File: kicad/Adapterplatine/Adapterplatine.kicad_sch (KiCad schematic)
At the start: 38 parts, among them J1 Conn_02x10_Top_Bottom, J10 Conn_01x04_Pin, J11 Conn_01x03_Pin, J12 Conn_01x02_Pin, J13 Conn_01x05_Pin, J14 Conn_01x02_Pin, J15 Conn_01x02_Pin, J16 Conn_01x05_Pin, J17 Conn_01x05_Pin, J18 Conn_01x05_Pin, J19 Conn_01x05_Pin, J2 DE9_Socket, J20 Conn_01x05_Pin, J21 Conn_01x05_Pin, J22 Conn_01x02_Pin, J23 Conn_01x02_Pin, J24 Conn_01x02_Pin, J25 Conn_01x02_Pin, J26 Conn_01x02_Pin, J27 Conn_01x05_Pin, J28 Conn_01x05_Pin, J29 Conn_01x02_Pin, J3 DE9_Pins, J30 Conn_01x05_Pin, J31 Conn_01x05_Pin, J32 Conn_01x05_Pin, J33 Conn_02x05_Top_Bottom, J34 Conn_01x02_Pin, J35 Conn_01x02_Pin, J4 DE9_Pins, J5 Conn_01x04_Pin, J6 Conn_01x04_Pin, J7 Conn_01x04_Pin, J8 Conn_01x04_Pin, J9 Conn_01x04_Pin

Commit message: Update KiCad
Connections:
- net at R3.1: now also R1.1, R2.1
- net GND: now reaches J35.2 (Pin_2)
- net GND: now also J33.5 (Pin_5), J34.2 (Pin_2)
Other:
- moved on the sheet: R1, R2, R3

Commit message: Adapterplatine weitergeführt/ Doku F421
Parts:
- added FAN0, FAN1, FAN2, X38__1, X44__g1, X44__r1, X48__PT1000_1, X48__PT1000_2: Conn_01x02_Pin, Connector_JST:JST_XH_B2B-XH-A_1x02_P2.50mm_Vertical, symbol Connector:Conn_01x02_Pin
- added I2C1: Conn_01x04_Pin, Connector_PinHeader_2.54mm:PinHeader_1x04_P2.54mm_Vertical, symbol Connector:Conn_01x04_Pin
- added Raspi_1, Raspi_2: Conn_01x05_Pin, Connector_PinHeader_2.54mm:PinHeader_1x05_P2.54mm_Vertical, symbol Connector:Conn_01x05_Pin
- added X10__1, X9__1: Conn_01x04_Pin, Connector_JST:JST_XH_B4B-XH-A_1x04_P2.50mm_Vertical, symbol Connector:Conn_01x04_Pin
- added X12__1, X13__1, X15__1, X37__1, X39__1, X48__Servo1, X_EndStop4, X_EndStop5, X_EndStop6: Conn_01x03_Pin, Connector_JST:JST_XH_B3B-XH-A_1x03_P2.50mm_Vertical, symbol Connector:Conn_01x03_Pin
- added X1__1, X3__1: Conn_01x02_Pin, Connector_Phoenix_MSTB:PhoenixContact_MSTBA_2,5_2-G_1x02_P5.00mm_Horizontal, symbol Connector:Conn_01x02_Pin
- added X44__y1, X44_b1: Conn_01x04_Pin, Connector_Molex:Molex_KK-254_AE-6410-04A_1x04_P2.54mm_Vertical, symbol Connector:Conn_01x04_Pin
- added X46__1: Conn_02x05_Top_Bottom, Connector_IDC:IDC-Header_2x05_P2.54mm_Vertical, symbol Connector_Generic:Conn_02x05_Top_Bottom
- added X5__1, X6__1, X7__1: Conn_01x04_Pin, Connector_JST:JST_VH_B4P-VH_1x04_P3.96mm_Vertical, symbol Connector:Conn_01x04_Pin
- X46: renamed from J33; footprint Connector_PinHeader_2.54mm:PinHeader_2x05_P2.54mm_Vertical -> Connector_IDC:IDC-Header_2x05_P2.54mm_Vertical
- renumbered J13 to J2, J10 to J3, J11 to J4, R1 to R_X12, R2 to R_X13, R3 to R_X15, J34 to X1, J6 to X10, J19 to X12, J20 to X13, J31 to X15, J21 to X16, J15 to X20, J12 to X22, J22 to X23, J29 to X25_1, J18 to X28_1, J32 to X29_1, J35 to X3, J16 to X30, J17 to X31, J3 to X36A1, J2 to X36B1, J25 to X37, J23 to X38, J24 to X39, J14 to X40, J28 to X43, J27 to X44, J4 to X45, J1 to X48, J7 to X5, J30 to X52, J26 to X56, J8 to X6, J9 to X7, J5 to X9
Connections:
- net GND: now also X12.2 (Pin_2), X12.4 (Pin_4), X13.2 (Pin_2), X13.4 (Pin_4), X15.2 (Pin_2), X15.4 (Pin_4), X29_1.1 (Pin_1), X29_1.5 (Pin_5), I2C1.2 (Pin_2), Raspi_1.3 (Pin_3), Raspi_2.3 (Pin_3), X12__1.2 (Pin_2), X13__1.2 (Pin_2), X15__1.2 (Pin_2), X1__1.2 (Pin_2), X3__1.2 (Pin_2), X46__1.6 (Pin_6)
- net at R_X15.2: now also X15.1 (Pin_1)
- net at X44.1 (Pin_1): now also X44_b1.1 (Pin_1)
- net at X44.2 (Pin_2): now also X44__g1.1 (Pin_1), X44__r1.1 (Pin_1), X44__y1.3 (Pin_3), X44_b1.3 (Pin_3)
- net at X44.3 (Pin_3): now also X44__y1.1 (Pin_1)
- net at X44.4 (Pin_4): now also X44__g1.2 (Pin_2)
- net at X44.5 (Pin_5): now also X44__r1.2 (Pin_2)
- net at X29_1.2 (Pin_2): now also I2C1.1 (Pin_1)
- net at X29_1.3 (Pin_3): now also I2C1.3 (Pin_3)
- net at X29_1.4 (Pin_4): now also I2C1.4 (Pin_4)
- net at X9.1 (Pin_1): now also X9__1.2 (Pin_2)
- net at X9.2 (Pin_2): now also X9__1.1 (Pin_1)
- net at X9.3 (Pin_3): now also X9__1.4 (Pin_4)
- net at X9.4 (Pin_4): now also X9__1.3 (Pin_3)
- net at X10.1 (Pin_1): now also X10__1.2 (Pin_2)
- net at X10.2 (Pin_2): now also X10__1.1 (Pin_1)
- net at X10.3 (Pin_3): now also X10__1.4 (Pin_4)
- net at X10.4 (Pin_4): now also X10__1.3 (Pin_3)
- net at X3.1 (Pin_1): now also X3__1.1 (Pin_1)
- net at X12.1 (Pin_1): now also R_X12.1
- net at X12.5 (Pin_5): now also X12__1.3 (Pin_3)
- net at R_X13.2: now also X13__1.1 (Pin_1)
- net at X37.1 (Pin_1): now also X37__1.2 (Pin_2)
- net at X37.2 (Pin_2): now also X37__1.3 (Pin_3)
- net at X39.1 (Pin_1): now also X39__1.2 (Pin_2)
- net at X39.2 (Pin_2): now also X39__1.3 (Pin_3)
- net at X7.1 (Pin_1): now also X7__1.2 (Pin_2)
- net at X7.2 (Pin_2): now also X7__1.1 (Pin_1)
- net at X7.3 (Pin_3): now also X7__1.4 (Pin_4)
- net at X7.4 (Pin_4): now also X7__1.3 (Pin_3)
- net GND TOOL: now reaches X48.1 (Pin_1)
- net GND TOOL: now also X48.15 (Pin_15), X48.16 (Pin_16), X48.2 (Pin_2), X48.8 (Pin_8)
- net at X48.10 (Pin_10): now also X48__Servo1.1 (Pin_1)
- net VIN Tool1: now reaches X48.11 (Pin_11)
- net VIN Tool1: now also X48.12 (Pin_12)
- net at X48.13 (Pin_13): now also X48__PT1000_1.2 (Pin_2)
- net at X48.14 (Pin_14): now also X48__PT1000_2.2 (Pin_2)
- net VIN Tool0: now reaches X48.17 (Pin_17)
- net VIN Tool0: now also X48.18 (Pin_18)
- net at X48.19 (Pin_19): now also X48__PT1000_2.1 (Pin_1)
- net at X48.20 (Pin_20): now also X48__PT1000_1.1 (Pin_1)
- net at X48.4 (Pin_4): now also FAN1.1 (Pin_1)
- net at X48.6 (Pin_6): now also FAN2.2 (Pin_2)
- net at X48.7 (Pin_7): now also X48__Servo1.2 (Pin_2)
- net at X48.9 (Pin_9): now also FAN1.2 (Pin_2), FAN2.1 (Pin_1), X48__Servo1.3 (Pin_3)
- net at X15.5 (Pin_5): now also X15__1.3 (Pin_3)
- net at X13.1 (Pin_1): now also R_X13.1
- net at X13.5 (Pin_5): now also X13__1.3 (Pin_3)
- net at X1.1 (Pin_1): now also X1__1.1 (Pin_1)
- net at X46.1 (Pin_1): now also X46__1.1 (Pin_1)
- net at X46.10 (Pin_10): now also X46__1.10 (Pin_10)
- net at X46.2 (Pin_2): now also X46__1.2 (Pin_2)
- net at X46.3 (Pin_3): now also X46__1.3 (Pin_3)
- net at X46.7 (Pin_7): now also X46__1.7 (Pin_7)
- net at R_X12.2: now also X12__1.1 (Pin_1)
- net at X5.1 (Pin_1): now also X5__1.2 (Pin_2)
- net at X5.2 (Pin_2): now also X5__1.1 (Pin_1)
- net at X5.3 (Pin_3): now also X5__1.4 (Pin_4)
- net at X5.4 (Pin_4): now also X5__1.3 (Pin_3)
- net at X38.1 (Pin_1): now also X38__1.1 (Pin_1)
- net at X38.2 (Pin_2): now also X38__1.2 (Pin_2)
- net at X6.1 (Pin_1): now also X6__1.2 (Pin_2)
- net at X6.2 (Pin_2): now also X6__1.1 (Pin_1)
- net at X6.3 (Pin_3): now also X6__1.4 (Pin_4)
- net at X6.4 (Pin_4): now also X6__1.3 (Pin_3)
- new net: R_X15.1, X15__1.1 (Pin_1)
- new net: Raspi_1.1 (Pin_1), Raspi_2.1 (Pin_1)
- new net: Raspi_1.2 (Pin_2), Raspi_2.2 (Pin_2)
- new net: Raspi_1.4 (Pin_4), Raspi_2.4 (Pin_4)
- new net: Raspi_1.5 (Pin_5), Raspi_2.5 (Pin_5)
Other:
- moved on the sheet: R_X12, R_X13, R_X15, X12, X13, X15, X16, X23, X25_1, X28_1, X29_1, X37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

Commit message: Doku F421/ Klipper ython modul erstellt/ KiCad Adapterplatine
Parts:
- added X48_Tool0, X48_Tool1: Conn_01x02_Pin, Connector_Phoenix_MSTB:PhoenixContact_MSTBA_2,5_2-G_1x02_P5.00mm_Horizontal, symbol Connector:Conn_01x02_Pin
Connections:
- net GND TOOL: now also X48_Tool0.1 (Pin_1), X48_Tool1.1 (Pin_1)
- net VIN Tool0: now also X48_Tool0.2 (Pin_2)
- net VIN Tool1: now also X48_Tool1.2 (Pin_2)

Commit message: Adapterplatinen Update
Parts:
- removed X_EndStop4, X_EndStop5: Conn_01x03_Pin, Connector_JST:JST_XH_B3B-XH-A_1x03_P2.50mm_Vertical, symbol Connector:Conn_01x03_Pin
- added MAX31865_IN1: Conn_01x08_Pin, Connector_PinSocket_2.54mm:PinSocket_1x08_P2.54mm_Vertical, symbol Connector:Conn_01x08_Pin
- added MAX31865_OUT1: Conn_01x04_Pin, Connector_PinSocket_2.54mm:PinSocket_1x04_P2.54mm_Vertical, symbol Connector:Conn_01x04_Pin
- added PowerOn1: Conn_01x02_Pin, Connector_PinHeader_2.54mm:PinHeader_1x02_P2.54mm_Vertical, symbol Connector:Conn_01x02_Pin
- added SPI4: Conn_02x04_Top_Bottom, Connector_PinHeader_2.54mm:PinHeader_2x04_P2.54mm_Vertical, symbol Connector_Generic:Conn_02x04_Top_Bottom
- added T_Bauraum1, T_HeizE1, T_Heizbett1: Conn_01x02_Pin, Connector_JST:JST_XH_B2B-XH-A_1x02_P2.50mm_Vertical, symbol Connector:Conn_01x02_Pin
- renumbered X_EndStop6 to Not_Aus1
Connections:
- net GND: now also X43.1 (Pin_1), MAX31865_IN1.2 (Pin_2), SPI4.1 (Pin_1), SPI4.4 (Pin_4)
- net at X29_1.2 (Pin_2): no longer I2C1.1 (Pin_1)
- net at X29_1.3 (Pin_3): now also I2C1.4 (Pin_4); no longer I2C1.3 (Pin_3)
- net at X29_1.4 (Pin_4): now also I2C1.3 (Pin_3); no longer I2C1.4 (Pin_4)
- net at FAN0.1 (Pin_1): now also X25_1.1 (Pin_1)
- net at FAN0.2 (Pin_2): now also X25_1.2 (Pin_2)
- net at X23.1 (Pin_1): now also T_Bauraum1.1 (Pin_1)
- net at X23.2 (Pin_2): now also T_Bauraum1.2 (Pin_2)
- net at X20.1 (Pin_1): now also T_HeizE1.1 (Pin_1)
- net at X20.2 (Pin_2): now also T_HeizE1.2 (Pin_2)
- net at X43.2 (Pin_2): now also PowerOn1.1 (Pin_1)
- net at X43.4 (Pin_4): now also PowerOn1.2 (Pin_2)
- net at X43.5 (Pin_5): now also I2C1.1 (Pin_1), SPI4.8 (Pin_8)
- net at X22.1 (Pin_1): now also MAX31865_OUT1.2 (Pin_2)
- net at X22.2 (Pin_2): now also MAX31865_OUT1.3 (Pin_3)
- net at Not_Aus1.2 (Pin_2): now also X16.4 (Pin_4)
- net at Not_Aus1.3 (Pin_3): now also X16.5 (Pin_5)
- net at X56.1 (Pin_1): now also T_Heizbett1.1 (Pin_1)
- net at X56.2 (Pin_2): now also T_Heizbett1.2 (Pin_2)
- new net: MAX31865_IN1.4 (Pin_4), SPI4.2 (Pin_2)
- new net: MAX31865_IN1.5 (Pin_5), SPI4.3 (Pin_3)
- new net: MAX31865_IN1.1 (Pin_1), SPI4.5 (Pin_5)
- new net: MAX31865_IN1.7 (Pin_7), SPI4.6 (Pin_6)
- new net: MAX31865_IN1.6 (Pin_6), SPI4.7 (Pin_7)
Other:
- moved on the sheet: FAN0, Not_Aus1, Raspi_1

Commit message: Kicad update
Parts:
- FAN0, FAN1, FAN2, PowerOn1, T_Bauraum1, T_HeizE1, T_Heizbett1, X1, X1__1, X20, X22, X23, X25_1, X3, X37, X38, X38__1, X39, X3__1, X40, X44__g1, X44__r1, X48_Tool0, X48_Tool1, X48__PT1000_1, X48__PT1000_2, X56: symbol Connector:Conn_01x02_Pin -> Connector_Generic:Conn_01x02
- J2, Raspi_1, Raspi_2, X12, X13, X15, X16, X28_1, X29_1, X30, X31, X43, X44, X52: symbol Connector:Conn_01x05_Pin -> Connector_Generic:Conn_01x05
- X36A1, X45: symbol Connector:DE9_Pins -> Connector:DE9_Pins_MountingHoles
- X36B1: symbol Connector:DE9_Socket -> Connector:DE9_Socket_MountingHoles
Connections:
- net GND: no longer X15.2 (Pin_2), X15.4 (Pin_4), X29_1.1 (Pin_1), X29_1.5 (Pin_5)
- net at R_X15.2: no longer X15.1 (Pin_1)
- net at X29_1.3 (Pin_3): no longer I2C1.4 (Pin_4)
- net at X29_1.4 (Pin_4): no longer I2C1.3 (Pin_3)
- net +5V: now reaches I2C1.1 (Pin_1), SPI4.8 (Pin_8), X43.5 (Pin_5)
- net +5V: now also R_X13.1, X13.1 (Pin_1)
- net at Not_Aus1.2 (Pin_2), X16.4 (Pin_4): now also X16.3 (Pin_3)
- net at X15.5 (Pin_5): no longer X15__1.3 (Pin_3)
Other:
- moved on the sheet: J3, J4, Not_Aus1, R_X12, R_X13, X12__1, X13__1, X37__1, X39__1, X44__y1, X44_b1

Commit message: Adapterplatine sortiert
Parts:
- removed FAN0, FAN1, FAN2, T_Bauraum1, T_HeizE1, T_Heizbett1, X38__1, X44__g1, X44__r1, X48__PT1000_1, X48__PT1000_2: Conn_01x02_Pin, Connector_JST:JST_XH_B2B-XH-A_1x02_P2.50mm_Vertical, symbol Connector_Generic:Conn_01x02
- removed I2C1, J3: Conn_01x04_Pin, Connector_PinHeader_2.54mm:PinHeader_1x04_P2.54mm_Vertical, symbol Connector:Conn_01x04_Pin
- removed J2, Raspi_1, Raspi_2, X12, X13, X15, X16, X28_1, X29_1, X30, X31, X43, X44: Conn_01x05_Pin, Connector_PinHeader_2.54mm:PinHeader_1x05_P2.54mm_Vertical, symbol Connector_Generic:Conn_01x05
- removed J4: Conn_01x03_Pin, Connector_PinHeader_2.54mm:PinHeader_1x03_P2.54mm_Vertical, symbol Connector:Conn_01x03_Pin
- removed MAX31865_IN1: Conn_01x08_Pin, Connector_PinSocket_2.54mm:PinSocket_1x08_P2.54mm_Vertical, symbol Connector:Conn_01x08_Pin
- removed MAX31865_OUT1: Conn_01x04_Pin, Connector_PinSocket_2.54mm:PinSocket_1x04_P2.54mm_Vertical, symbol Connector:Conn_01x04_Pin
- removed Not_Aus1, X12__1, X13__1, X15__1, X37__1, X39__1, X48__Servo1: Conn_01x03_Pin, Connector_JST:JST_XH_B3B-XH-A_1x03_P2.50mm_Vertical, symbol Connector:Conn_01x03_Pin
- removed PowerOn1, X20, X22, X23, X25_1, X37, X38, X39, X56: Conn_01x02_Pin, Connector_PinHeader_2.54mm:PinHeader_1x02_P2.54mm_Vertical, symbol Connector_Generic:Conn_01x02
- removed R_X12, R_X13, R_X15: 220, Resistor_THT:R_Axial_DIN0207_L6.3mm_D2.5mm_P2.54mm_Vertical, symbol Device:R
- removed SPI4: Conn_02x04_Top_Bottom, Connector_PinHeader_2.54mm:PinHeader_2x04_P2.54mm_Vertical, symbol Connector_Generic:Conn_02x04_Top_Bottom
- removed X1, X1__1, X3, X3__1, X48_Tool0, X48_Tool1: Conn_01x02_Pin, Connector_Phoenix_MSTB:PhoenixContact_MSTBA_2,5_2-G_1x02_P5.00mm_Horizontal, symbol Connector_Generic:Conn_01x02
- removed X10, X5, X6, X7, X9: Conn_01x04_Pin, Connector_Phoenix_MSTB:PhoenixContact_MSTBVA_2,5_4-G-5,08_1x04_P5.08mm_Vertical, symbol Connector:Conn_01x04_Pin
- removed X10__1, X9__1: Conn_01x04_Pin, Connector_JST:JST_XH_B4B-XH-A_1x04_P2.50mm_Vertical, symbol Connector:Conn_01x04_Pin
- removed X36B1: DE9_Socket, Connector_Dsub:DSUB-9_Socket_Vertical_P2.77x2.84mm_MountingHoles, symbol Connector:DE9_Socket_MountingHoles
- removed X44__y1, X44_b1: Conn_01x04_Pin, Connector_Molex:Molex_KK-254_AE-6410-04A_1x04_P2.54mm_Vertical, symbol Connector:Conn_01x04_Pin
- removed X46, X46__1: Conn_02x05_Top_Bottom, Connector_IDC:IDC-Header_2x05_P2.54mm_Vertical, symbol Connector_Generic:Conn_02x05_Top_Bottom
- removed X48: Conn_02x10_Top_Bottom, Connector_Molex:Molex_Micro-Fit_3.0_43045-2012_2x10_P3.00mm_Vertical, symbol Connector_Generic:Conn_02x10_Top_Bottom
- removed X5__1, X6__1, X7__1: Conn_01x04_Pin, Connector_JST:JST_VH_B4P-VH_1x04_P3.96mm_Vertical, symbol Connector:Conn_01x04_Pin
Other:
- added sheet Fan (fan.kicad_sch)
- added sheet Limit Switches (limitswitches.kicad_sch)
- added sheet Motor Driver (motordriver.kicad_sch)
- added sheet Power (power.kicad_sch)
- added sheet Raspberry PI (raspi.kicad_sch)
- added sheet platines (platines.kicad_sch)
- added sheet temperature (temp.kicad_sch)
- moved on the sheet: X40, X52

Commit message: Bessere Verlegungen Adapterplatine
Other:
- sheet platines ports: added +3.3V; removed none
- sheet temperature ports: added +3.3V; removed none
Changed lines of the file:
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@@
+	(wire
+		(pts
+			(xy 74.93 52.07) (xy 109.22 52.07)
+		)
+		(stroke
+			(width 0)
+			(type default)
+		)
+	)
 	(wire
 		(pts
@@
 			)
 		)
+		(pin "+3.3V" input
+			(at 74.93 52.07 0)
+			(effects
+				(font
+					(size 1.27 1.27)
+				)
+				(justify right)
+			)
+		)
 		(instances
 			(project "Adapterplatine"
@@
 			(effects
 				(font
+					(size 1.27 1.27)
+				)
+				(justify left)
+			)
+		)
+		(pin "+3.3V" output
+			(at 109.22 52.07 180)
+			(effects
+				(font

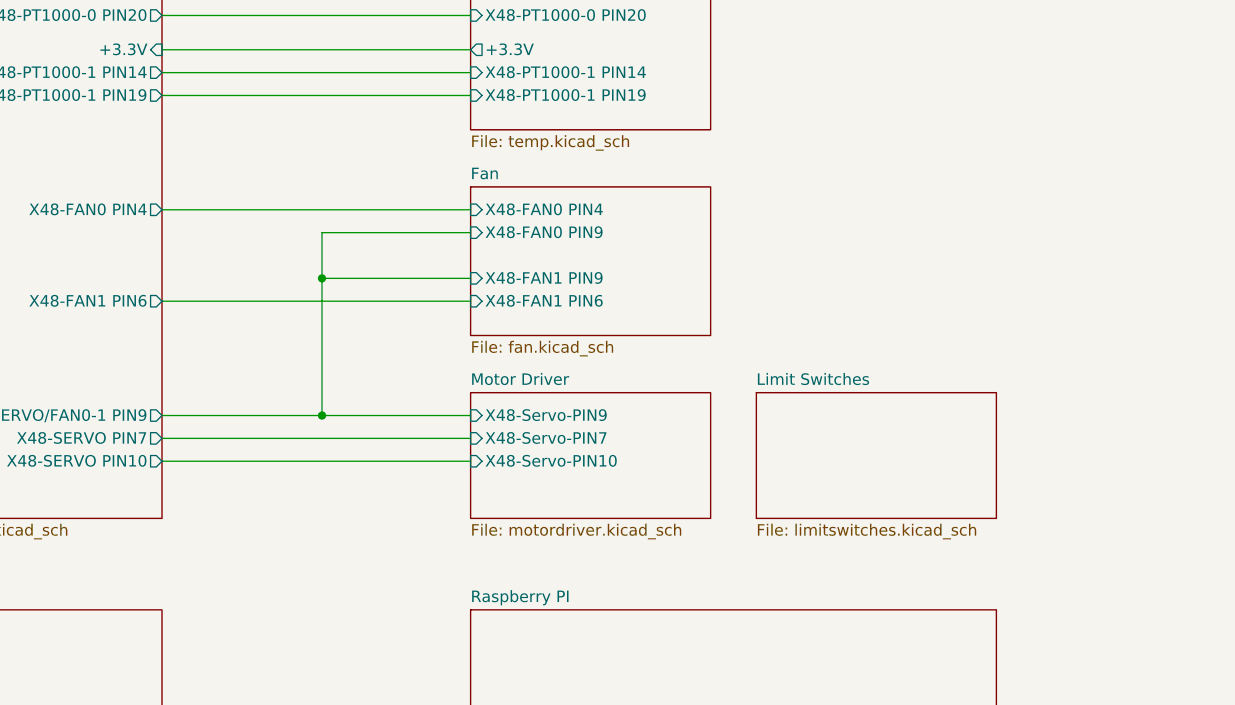
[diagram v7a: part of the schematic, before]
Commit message: Einbau Vakuum Pumpe/ Einzeichnung Kraken benutze Pins
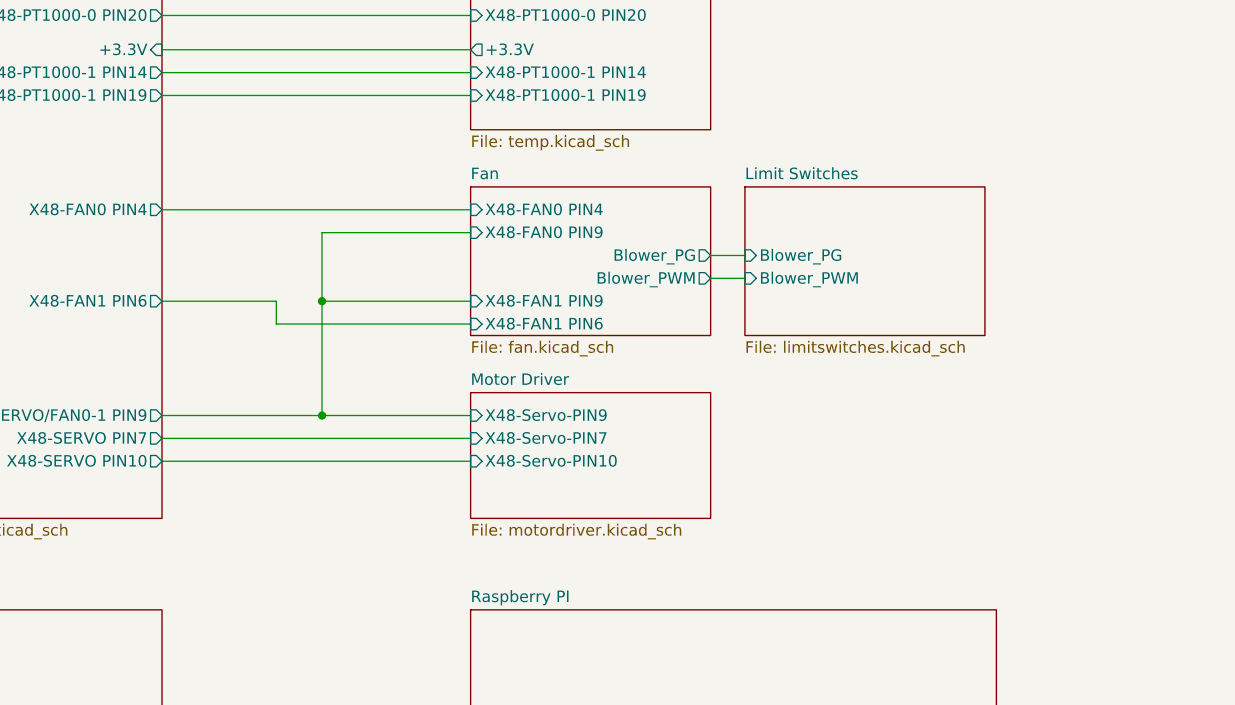
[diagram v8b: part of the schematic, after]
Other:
- sheet Fan ports: added Blower_PG, Blower_PWM; removed none
- sheet Limit Switches ports: added Blower_PG, Blower_PWM; removed none
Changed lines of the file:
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@@
 	(paper "A4")
-	(junction
-		(at 92.71 77.47)
-		(diameter 0)
-		(color 0 0 0 0)
-	)
 	(junction
 		(at 92.71 92.71)
@@
 		(color 0 0 0 0)
 	)
+	(junction
+		(at 92.71 80.01)
+		(diameter 0)
+		(color 0 0 0 0)
+	)
+	(wire
+		(pts
+			(xy 135.89 74.93) (xy 139.7 74.93)
+		)
+		(stroke
+			(width 0)
+			(type default)
+		)
+	)
+	(wire
+		(pts
+			(xy 92.71 80.01) (xy 92.71 92.71)
+		)
+		(stroke
+			(width 0)
+			(type default)
+		)
+	)
 	(wire
 		(pts
@@
 	(wire
 		(pts
-			(xy 92.71 77.47) (xy 109.22 77.47)
+			(xy 92.71 80.01) (xy 109.22 80.01)
 		)
 		(stroke
@@
 	(wire
 		(pts
-			(xy 74.93 80.01) (xy 109.22 80.01)
-		)
-		(stroke
-			(width 0)
-			(type default)
-		)
-	)
-	(wire
-		(pts
 			(xy 109.22 72.39) (xy 92.71 72.39)
 		)
@@
 	(wire
 		(pts
+			(xy 135.89 77.47) (xy 139.7 77.47)
+		)
+		(stroke
+			(width 0)
+			(type default)
+		)
+	)
+	(wire
+		(pts
 			(xy 74.93 48.26) (xy 109.22 48.26)
 		)
@@
 	(wire
 		(pts
+			(xy 109.22 82.55) (xy 87.63 82.55)
+		)
+		(stroke
+			(width 0)
+			(type default)
+		)
+	)
+	(wire
+		(pts
+			(xy 87.63 82.55) (xy 87.63 80.01)
+		)
+		(stroke
+			(width 0)
+			(type default)
+		)
+	)
+	(wire
+		(pts
 			(xy 74.93 95.25) (xy 109.22 95.25)
 		)
@@
 	(wire
 		(pts
+			(xy 87.63 80.01) (xy 74.93 80.01)
+		)
+		(stroke
+			(width 0)
+			(type default)
+		)
+	)
+	(wire
+		(pts
 			(xy 74.93 45.72) (xy 109.22 45.72)
 		)
@@
 	(wire
 		(pts
-			(xy 92.71 72.39) (xy 92.71 77.47)
-		)
-		(stroke
-			(width 0)
-			(type default)
-		)
-	)
-	(wire
-		(pts
 			(xy 74.93 69.85) (xy 109.22 69.85)
 		)
@@
 	(wire
 		(pts
-			(xy 92.71 77.47) (xy 92.71 92.71)
+			(xy 92.71 72.39) (xy 92.71 80.01)
 		)
 		(stroke
@@
 	)
 	(sheet
-		(at 140.97 90.17)
-		(size 26.67 13.97)
+		(at 139.7 67.31)
+		(size 26.67 16.51)
 		(exclude_from_sim no)
 		(in_bom yes)
@@
 		)
 		(property "Sheetname" "Limit Switches"
-			(at 140.97 89.4584 0)
+			(at 139.7 66.5984 0)
 			(show_name no)
 			(do_not_autoplace no)
@@
 		)
 		(property "Sheetfile" "limitswitches.kicad_sch"
-			(at 140.97 104.7246 0)
+			(at 139.7 84.4046 0)
 			(show_name no)
 			(do_not_autoplace no)
@@
 				)
 				(justify left top)
+			)
+		)
+		(pin "Blower_PG" input
+			(at 139.7 74.93 180)
+			(effects
+				(font
+					(size 1.27 1.27)
+				)
+				(justify left)
+			)
+		)
+		(pin "Blower_PWM" input
+			(at 139.7 77.47 180)
+			(effects
+				(font
+					(size 1.27 1.27)
+				)
+				(justify left)
 			)
 		)
@@
 		)
 		(pin "X48-FAN1 PIN6" input
+			(at 109.22 82.55 180)
+			(effects
+				(font
+					(size 1.27 1.27)
+				)
+				(justify left)
+			)
+		)
+		(pin "X48-FAN1 PIN9" input
 			(at 109.22 80.01 180)
 			(effects
@@
 			)
 		)
-		(pin "X48-FAN1 PIN9" input
-			(at 109.22 77.47 180)
-			(effects
-				(font
-					(size 1.27 1.27)
-				)
-				(justify left)
-			)
-		)
+		(pin "Blower_PG" output
+			(at 135.89 74.93 0)
+			(effects
+				(font
+					(size 1.27 1.27)
+				)
+				(justify right)
+			)
+		)
+		(pin "Blower_PWM" output
+			(at 135.89 77.47 0)
+			(effects
+				(font
+					(size 1.27 1.27)
+				)
+				(justify right)
+			)
+		)
